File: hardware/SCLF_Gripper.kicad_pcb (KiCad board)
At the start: 4 copper layers, 67.4 x 67.4 mm, 74 parts, among them J1 Conn_01x05, J2 Conn_01x03, J3 Coupling_02x05_Odd_Even, Q1 AO3401A, SW1 TSA002A3512A02, SW2 TSA002A3512A02, U1 DRV8316CRRGFR, U10 XC6206P332MR, U4 MAX3485, U8 MT6701QT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

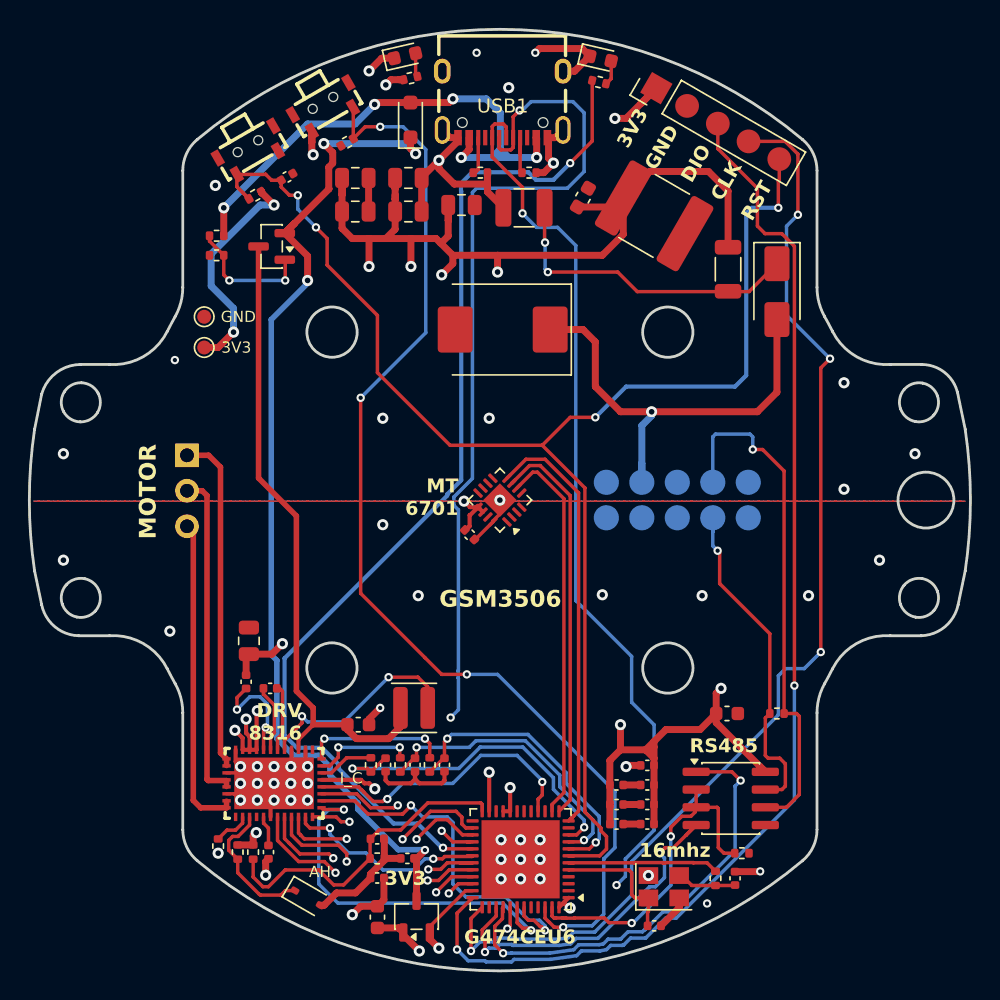
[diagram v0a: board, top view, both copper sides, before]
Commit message: docs: update pinout, images to PNG and hardware design files
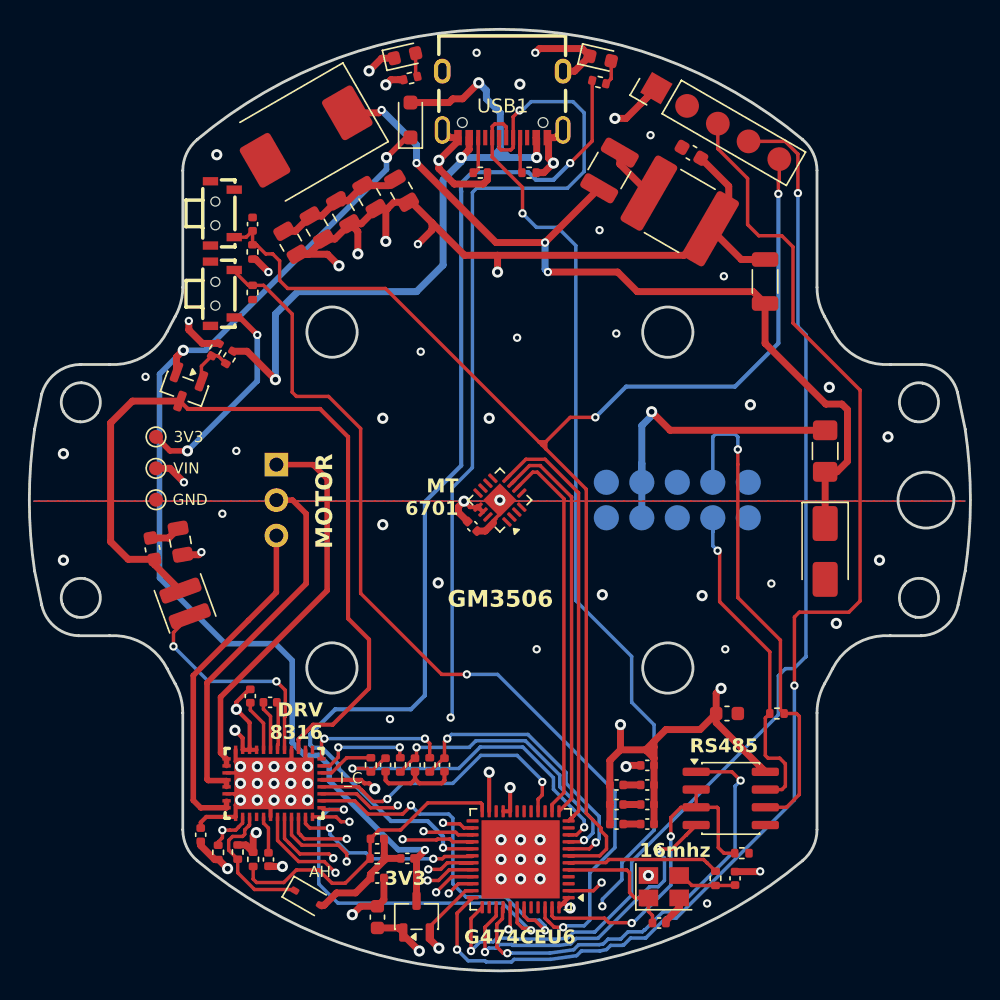
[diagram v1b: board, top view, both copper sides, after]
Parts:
- added C4: 100nF, Capacitor_SMD:C_0402_1005Metric, F.Cu at (111.0, 119.5)
- added F1: Fuse, Fuse:Fuse_1206_3216Metric_Pad1.42x1.75mm_HandSolder, F.Cu at (155.7, 92.0)
- added G: LOGO, Aimar:QR, B.Cu at (127.4, 95.5)
- added TP3: VIN, TestPoint:TestPoint_Pad_D1.0mm, F.Cu at (107.8, 93.2)
- J2: footprint Connector_PinHeader_2.54mm:PinHeader_1x03_P2.54mm_Vertical -> Aimar:PinHeader_1x03_P2.54mm_Vertical_Center
- moved D6 19.7 mm to (118.5, 69.5), turned to -150 degrees
- moved C35 19.4 mm to (107.5, 99.0), turned to 100 degrees
- moved D5 18.9 mm to (155.7, 99.2)
- moved L1 18.0 mm to (109.8, 102.9), turned to 110 degrees
- moved SW1 15.2 mm to (112.5, 80.8), turned to 90 degrees
- moved TP1 13.5 mm to (107.8, 95.5)
- moved R16 12.7 mm to (114.7, 80.7), turned to -90 degrees
- moved Q1 12.0 mm to (109.8, 87.6), turned to -110 degrees
- moved R33 8.76 mm to (113.0, 85.3), turned to 60 degrees
- moved C44 8.63 mm to (109.5, 98.5), turned to 100 degrees
- moved C3 8.40 mm to (146.1, 70.7), turned to 150 degrees
- moved TP2 7.27 mm to (107.8, 91.0)
- moved J2 7.16 mm to (116.4, 95.5)
- moved R32 6.75 mm to (112.0, 84.8), turned to -120 degrees
- moved C1 6.68 mm to (140.2, 71.9), turned to 60 degrees
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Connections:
- D5 pad 2: 24V -> GND
- D6 pad 1: 24V -> Net-(D5-A1)
- J3 pad 2: unconnected-(J3-Pin_2-Pad2) -> GND
- J3 pad 4: unconnected-(J3-Pin_4-Pad4) -> 24V
- L2 pad 1: VIN -> Net-(D5-A1)
- L2 pad 2: Net-(D5-A1) -> VIN
- R25 pad 2: Net-(U1-nFAULT) -> DRV_FAULT
- U1 pad 21: unconnected-(U1-DRVOFF-Pad21) -> GND
- U1 pad 22: Net-(U1-nFAULT) -> DRV_FAULT
- U9 pad 2: unconnected-(U9-PC13-Pad2) -> DRV_FAULT
- U9 pad 26: AL -> CL
- U9 pad 28: CL -> AL
- U9 pad 38: PA15 -> unconnected-(U9-PA15-Pad38)
- U9 pad 44: PB6 -> unconnected-(U9-PB6-Pad44)
- U9 pad 45: PB7 -> unconnected-(U9-PB7-Pad45)
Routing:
- net DRV_FAULT: track 0.00 -> 43.4 mm, vias 0 -> 2
- net Net-(D5-A1): track 23.6 -> 63.3 mm, vias 2 -> 4
- net BOOT0: track 81.0 -> 67.4 mm, vias 4 -> 2
- net BUCK: track 46.7 -> 59.8 mm
- net VBUS: track 38.9 -> 51.9 mm, vias 5 -> 4
- net GND: track 75.2 -> 87.3 mm, vias 54 -> 65
- net 24V: track 33.0 -> 22.2 mm
- net RST: track 105.5 -> 98.2 mm, vias 4 -> 2
- net SWDIO: track 85.6 -> 91.8 mm
- net VIN: track 76.5 -> 70.4 mm, vias 9 -> 10
- net Net-(Q1-G): track 9.33 -> 3.35 mm, vias 2 -> 0
- net Net-(U1-CP): track 7.99 -> 3.76 mm, vias 2 -> 0
- net PHA: track 24.3 -> 27.9 mm
- net PHB: track 23.7 -> 26.7 mm
- net Net-(U1-nFAULT): track 2.66 -> 0.00 mm
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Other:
- board text added: "GM3506"
- board text added: "SCLF_Gripper_v2.0"
- board text removed: "GSM3506"
- board text removed: "SCLF_Gripper_v1.0"
